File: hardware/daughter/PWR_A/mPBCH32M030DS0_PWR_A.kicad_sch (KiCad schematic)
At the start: 0 parts

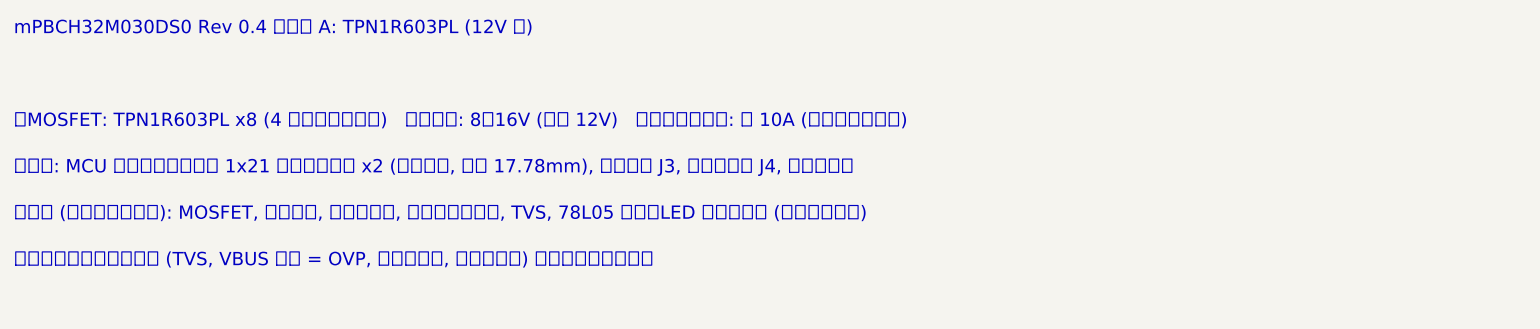
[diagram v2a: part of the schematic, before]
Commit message: 子基板 A/C: 電源の銅箔を配線前に置く再レイアウト (A 約4A/相, C 3A)
- レッグを LS/HS の縦ブロックにし, 下面 = ISH の背骨 + SRC/VBUS/SW の島,
  上面 = VBUS の帯と各相 SW の階段状の帯 (J4 は 180° 回転: OUT3 が上)
- 固定ベタは DSN では keepout (縁 0.3mm は同ネットの取り付き用) + via_keepout にして
  自動配線がベタを削らないようにした。2 段配線 (MPB_TWO_PHASE) も用意
- A: ゲート抵抗 (0805) の電極間を SW/GL が抜ける配置 (J2 の並びと FET のゲート位置の上下逆を解消)
- A/C: バルク容量は ISH 戻り (VBUS-ISH), USB 側 TVS (D9) は省略, NTC は下側へ
- 電流チェックに 1mm 平均の密度 (角の電流集中を除く) を追加
- ヒートシンクの干渉チェックは MOSFET の範囲だけに

Co-Authored-By: Claude Opus 5.5 <noreply@anthropic.com>
Claude-Session: https://claude.ai/code/session_01LENFjjhDfYjJZV1NWhB9uV
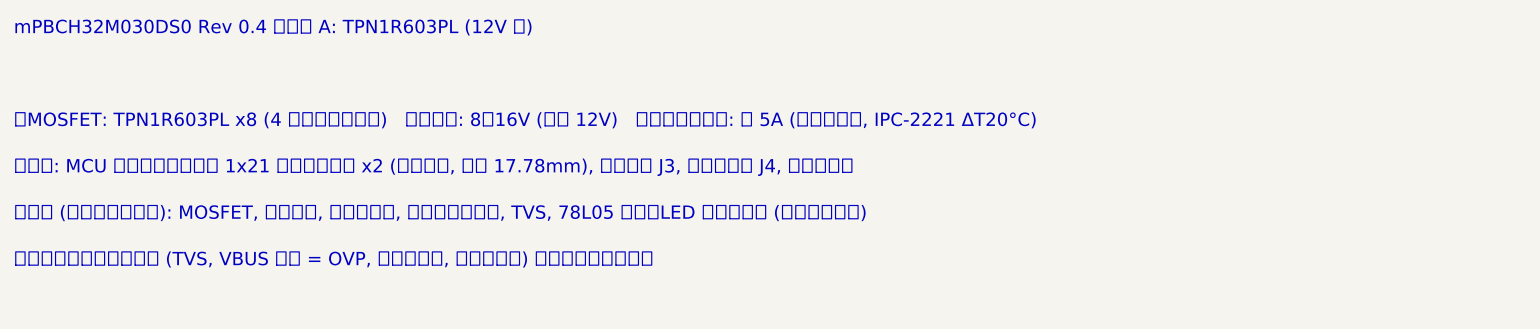
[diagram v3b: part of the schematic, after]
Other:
- note added: "・MOSFET: TPN1R603PL x8 (4 ハーフブリッジ) 入力電圧: 8〜16V (公称 12V) 出力電流の目安: 約 5A (銅箔幅律速, IPC-2221 ΔT20°C)"
- note removed: "・MOSFET: TPN1R603PL x8 (4 ハーフブリッジ) 入力電圧: 8〜16V (公称 12V) 出力電流の目安: 約 10A (ピンヘッダ律速)"
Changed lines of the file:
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@@
 (text "mPBCH32M030DS0 Rev 0.4 子基板 A: TPN1R603PL (12V 系)" (exclude_from_sim no) (at 20 30 0) (effects (font (size 2 2)) (justify left bottom)))
 (text "" (exclude_from_sim no) (at 20 37 0) (effects (font (size 2 2)) (justify left bottom)))
-(text "・MOSFET: TPN1R603PL x8 (4 ハーフブリッジ)   入力電圧: 8〜16V (公称 12V)   出力電流の目安: 約 10A (ピンヘッダ律速)" (exclude_from_sim no) (at 20 44 0) (effects (font (size 2 2)) (justify left bottom)))
+(text "・MOSFET: TPN1R603PL x8 (4 ハーフブリッジ)   入力電圧: 8〜16V (公称 12V)   出力電流の目安: 約 5A (銅箔幅律速, IPC-2221 ΔT20°C)" (exclude_from_sim no) (at 20 44 0) (effects (font (size 2 2)) (justify left bottom)))
 (text "・上面: MCU モジュールを挿す 1x21 ピンソケット x2 (左右対称, 列間 17.78mm), 電源入力 J3, モータ出力 J4, バルク容量" (exclude_from_sim no) (at 20 51 0) (effects (font (size 2 2)) (justify left bottom)))
 (text "・下面 (ヒートシンク側): MOSFET, シャント, ゲート抵抗, 理想ダイオード, TVS, 78L05 など。LED は置かない (モジュール側)" (exclude_from_sim no) (at 20 58 0) (effects (font (size 2 2)) (justify left bottom)))
